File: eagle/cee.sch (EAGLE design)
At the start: 56 parts, among them IC1 IC1, J1 SOLDERJUMPERNC2

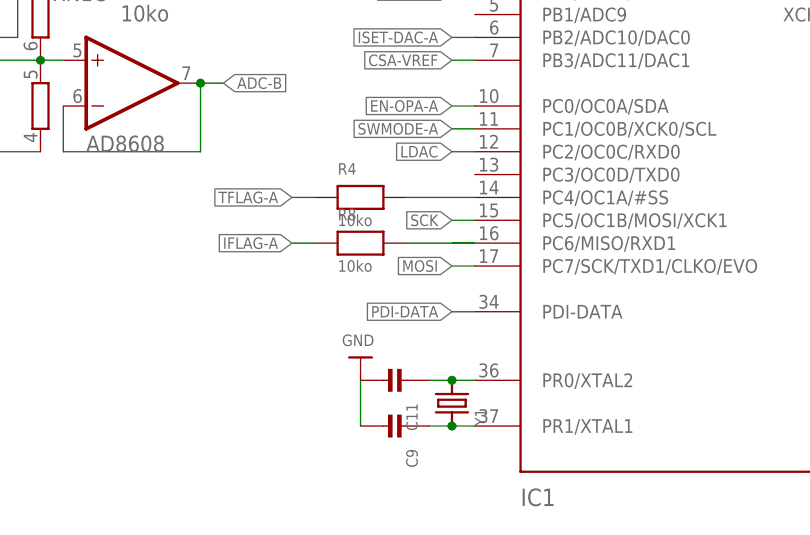
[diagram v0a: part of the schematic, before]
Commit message: Tweak expansion port labels.
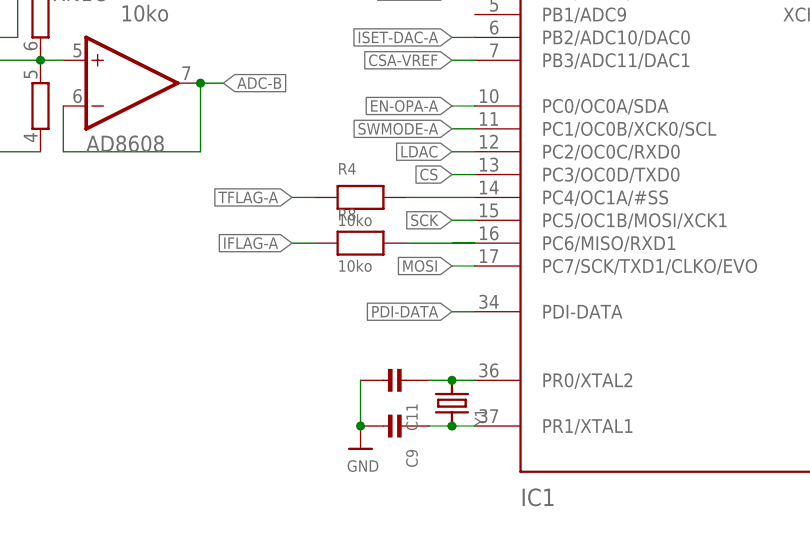
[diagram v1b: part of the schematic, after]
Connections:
- net CS: now also IC1.PC3/OC0D/TXD0
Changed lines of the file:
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@@
 <instance part="C9" gate="G$1" x="88.9" y="5.08" rot="R270"/>
 <instance part="C11" gate="G$1" x="88.9" y="10.16" rot="R270"/>
-<instance part="U$6" gate="G$1" x="86.36" y="12.7" rot="R180"/>
+<instance part="U$6" gate="G$1" x="86.36" y="2.54"/>
 <instance part="R1" gate="G$1" x="167.64" y="48.26" rot="R180"/>
 <instance part="R3" gate="G$1" x="167.64" y="50.8" rot="R180"/>
@@
 <label x="25.4" y="180.34" size="1.27" layer="95" rot="R180" xref="yes"/>
 </segment>
+<segment>
+<pinref part="IC1" gate="G$1" pin="PC3/OC0D/TXD0"/>
+<wire x1="99.06" y1="33.02" x2="96.52" y2="33.02" width="0.254" layer="91"/>
+<label x="96.52" y="33.02" size="1.27" layer="95" rot="R180" xref="yes"/>
+</segment>
 </net>
 <net name="SCK" class="0">
@@
 <pinref part="U$6" gate="G$1" pin="GND"/>
 <pinref part="C9" gate="G$1" pin="P$2"/>
+<junction x="86.36" y="5.08"/>
 <wire x1="86.36" y1="5.08" x2="86.36" y2="10.16" width="0.254" layer="91"/>
 </segment>

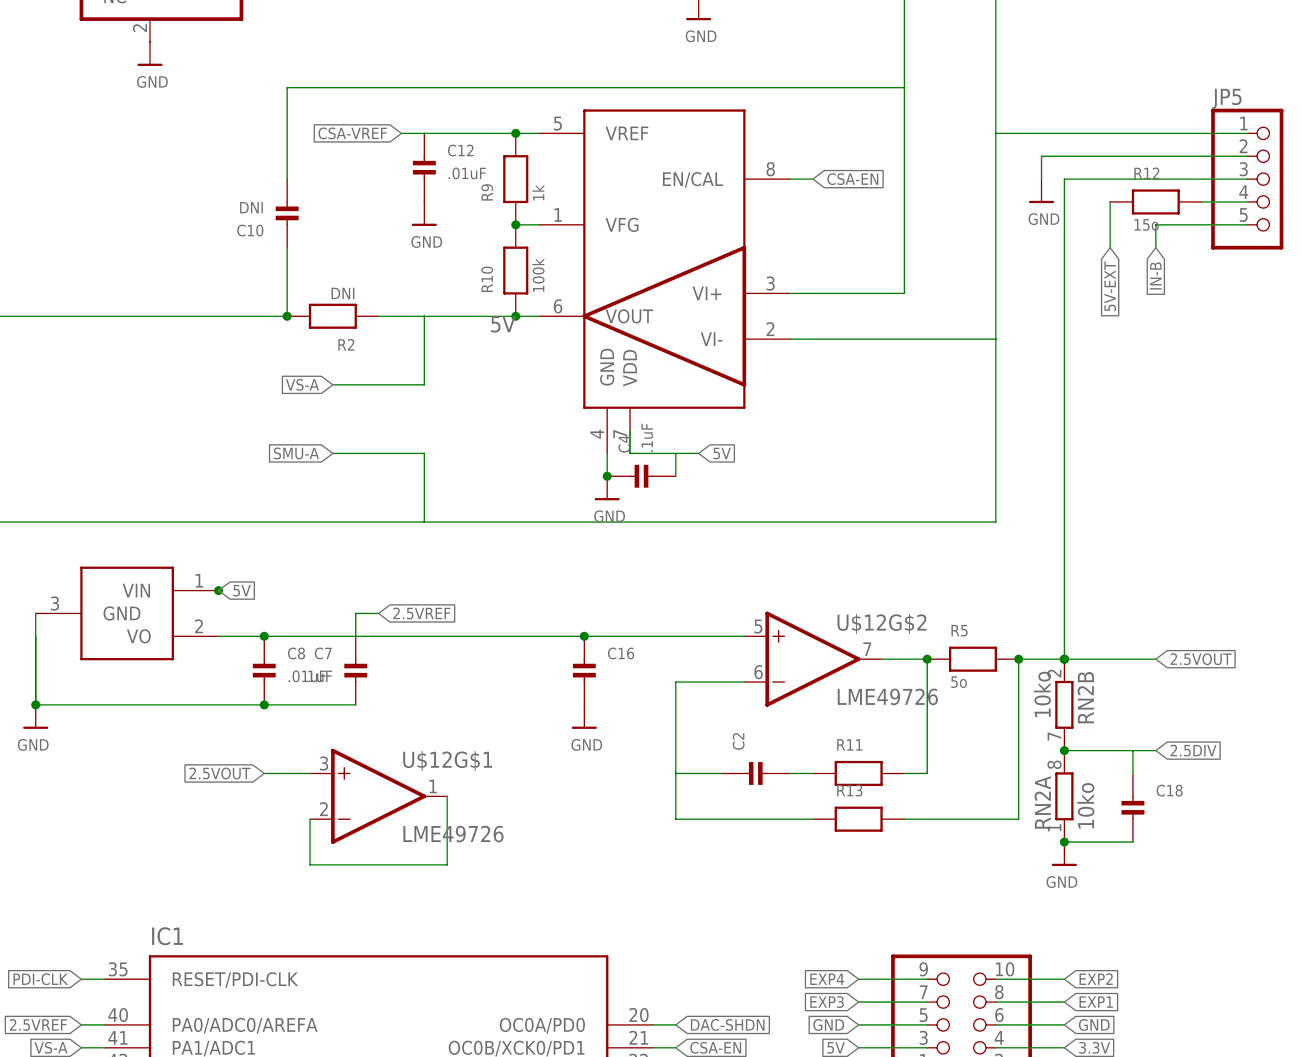
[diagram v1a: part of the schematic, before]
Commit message: Use LME49726 for current-limited 5V.
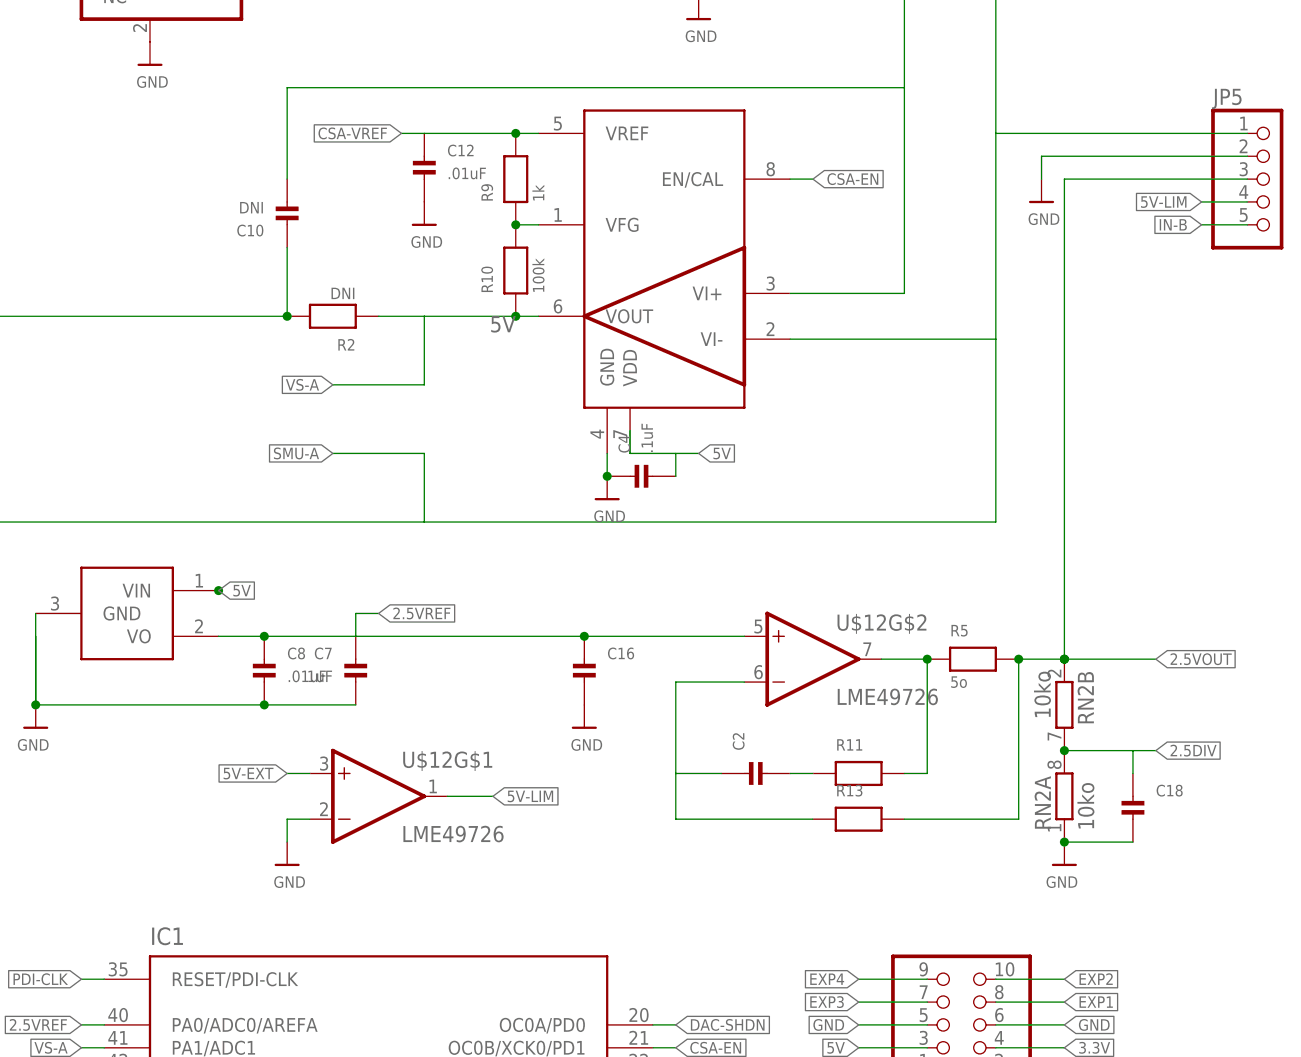
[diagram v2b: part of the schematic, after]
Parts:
- removed R12: 15o, nonolith:RESISTOR1206
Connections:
- removed net N$14: JP5.4, R12.2
- removed net N$15: U$12G$1.-IN, U$12G$1.OUT
- new net 5V-LIM: JP5.4, U$12G$1.OUT
- net 2.5VOUT: no longer U$12G$1.+IN
- net 5V-EXT: now also U$12G$1.+IN; no longer R12.1
- net GND: now also U$12G$1.-IN
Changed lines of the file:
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@@
 <part name="R11" library="nonolith" deviceset="RESISTOR" device="0603"/>
 <part name="C2" library="nonolith" deviceset="CAP_CERAMIC" device="0603"/>
-<part name="R12" library="nonolith" deviceset="RESISTOR" device="1206" value="15o"/>
 <part name="R13" library="nonolith" deviceset="RESISTOR" device="0603"/>
 <part name="R14" library="nonolith" deviceset="RESISTOR" device="0603" value="10k"/>
@@
 <part name="U$24" library="nonolith" deviceset="GND" device=""/>
 <part name="U$31" library="nonolith" deviceset="GND" device=""/>
+<part name="U$33" library="nonolith" deviceset="GND" device=""/>
 </parts>
 <sheets>
@@
 <instance part="R11" gate="G$1" x="182.88" y="106.68"/>
 <instance part="C2" gate="G$1" x="172.72" y="106.68" rot="R90"/>
-<instance part="R12" gate="G$1" x="215.9" y="170.18"/>
 <instance part="R13" gate="G$1" x="182.88" y="101.6"/>
 <instance part="R14" gate="G$1" x="86.36" y="198.12"/>
@@
 <instance part="RN2" gate="B" x="205.74" y="114.3" rot="R270"/>
 <instance part="U$31" gate="G$1" x="53.34" y="111.76"/>
+<instance part="U$33" gate="G$1" x="119.38" y="96.52"/>
 </instances>
 <busses>
@@
 <wire x1="27.94" y1="76.2" x2="25.4" y2="76.2" width="0.254" layer="91"/>
 </segment>
+<segment>
+<pinref part="U$12" gate="G$1" pin="-IN"/>
+<wire x1="121.92" y1="101.6" x2="119.38" y2="101.6" width="0.1524" layer="91"/>
+<wire x1="119.38" y1="101.6" x2="119.38" y2="99.06" width="0.1524" layer="91"/>
+<pinref part="U$33" gate="G$1" pin="GND"/>
+</segment>
 </net>
 <net name="PDI-DATA" class="0">
@@
 </segment>
 <segment>
-<pinref part="R12" gate="G$1" pin="1"/>
-<wire x1="210.82" y1="170.18" x2="210.82" y2="165.1" width="0.254" layer="91"/>
-<label x="210.82" y="165.1" size="1.27" layer="95" rot="R270" xref="yes"/>
+<pinref part="U$12" gate="G$1" pin="+IN"/>
+<wire x1="121.92" y1="106.68" x2="119.38" y2="106.68" width="0.1524" layer="91"/>
+<label x="119.38" y="106.68" size="1.27" layer="95" rot="R180" xref="yes"/>
 </segment>
 </net>
@@
 <junction x="205.74" y="119.38"/>
 </segment>
-<segment>
-<pinref part="U$12" gate="G$1" pin="+IN"/>
-<wire x1="121.92" y1="106.68" x2="116.84" y2="106.68" width="0.254" layer="91"/>
-<label x="116.84" y="106.68" size="1.27" layer="95" rot="R180" xref="yes"/>
-</segment>
 </net>
 <net name="2.5VFDBK" class="0">
@@
 <segment>
 <pinref part="JP5" gate="A" pin="5"/>
-<wire x1="226.06" y1="167.64" x2="215.9" y2="167.64" width="0.254" layer="91"/>
-<wire x1="215.9" y1="167.64" x2="215.9" y2="165.1" width="0.254" layer="91"/>
-<label x="215.9" y="165.1" size="1.27" layer="95" rot="R270" xref="yes"/>
+<wire x1="226.06" y1="167.64" x2="220.98" y2="167.64" width="0.254" layer="91"/>
+<label x="220.98" y="167.64" size="1.27" layer="95" rot="R180" xref="yes"/>
 </segment>
 <segment>
@@
 <pinref part="C2" gate="G$1" pin="P$2"/>
 <wire x1="177.8" y1="106.68" x2="175.26" y2="106.68" width="0.254" layer="91"/>
-</segment>
-</net>
-<net name="N$14" class="0">
-<segment>
-<pinref part="JP5" gate="A" pin="4"/>
-<wire x1="226.06" y1="170.18" x2="220.98" y2="170.18" width="0.254" layer="91"/>
-<pinref part="R12" gate="G$1" pin="2"/>
 </segment>
 </net>
@@
 </segment>
 </net>
-<net name="N$15" class="0">
-<segment>
-<pinref part="U$12" gate="G$1" pin="OUT"/>
-<wire x1="137.16" y1="104.14" x2="137.16" y2="96.52" width="0.254" layer="91"/>
-<pinref part="U$12" gate="G$1" pin="-IN"/>
-<wire x1="137.16" y1="96.52" x2="121.92" y2="96.52" width="0.254" layer="91"/>
-<wire x1="121.92" y1="96.52" x2="121.92" y2="101.6" width="0.254" layer="91"/>
-</segment>
-</net>
 <net name="BUFF-A" class="0">
 <segment>
@@
 </segment>
 </net>
+<net name="5V-LIM" class="0">
+<segment>
+<pinref part="U$12" gate="G$1" pin="OUT"/>
+<wire x1="137.16" y1="104.14" x2="142.24" y2="104.14" width="0.1524" layer="91"/>
+<label x="142.24" y="104.14" size="1.27" layer="95" xref="yes"/>
+</segment>
+<segment>
+<pinref part="JP5" gate="A" pin="4"/>
+<wire x1="226.06" y1="170.18" x2="220.98" y2="170.18" width="0.254" layer="91"/>
+<label x="220.98" y="170.18" size="1.27" layer="95" rot="R180" xref="yes"/>
+</segment>
+</net>

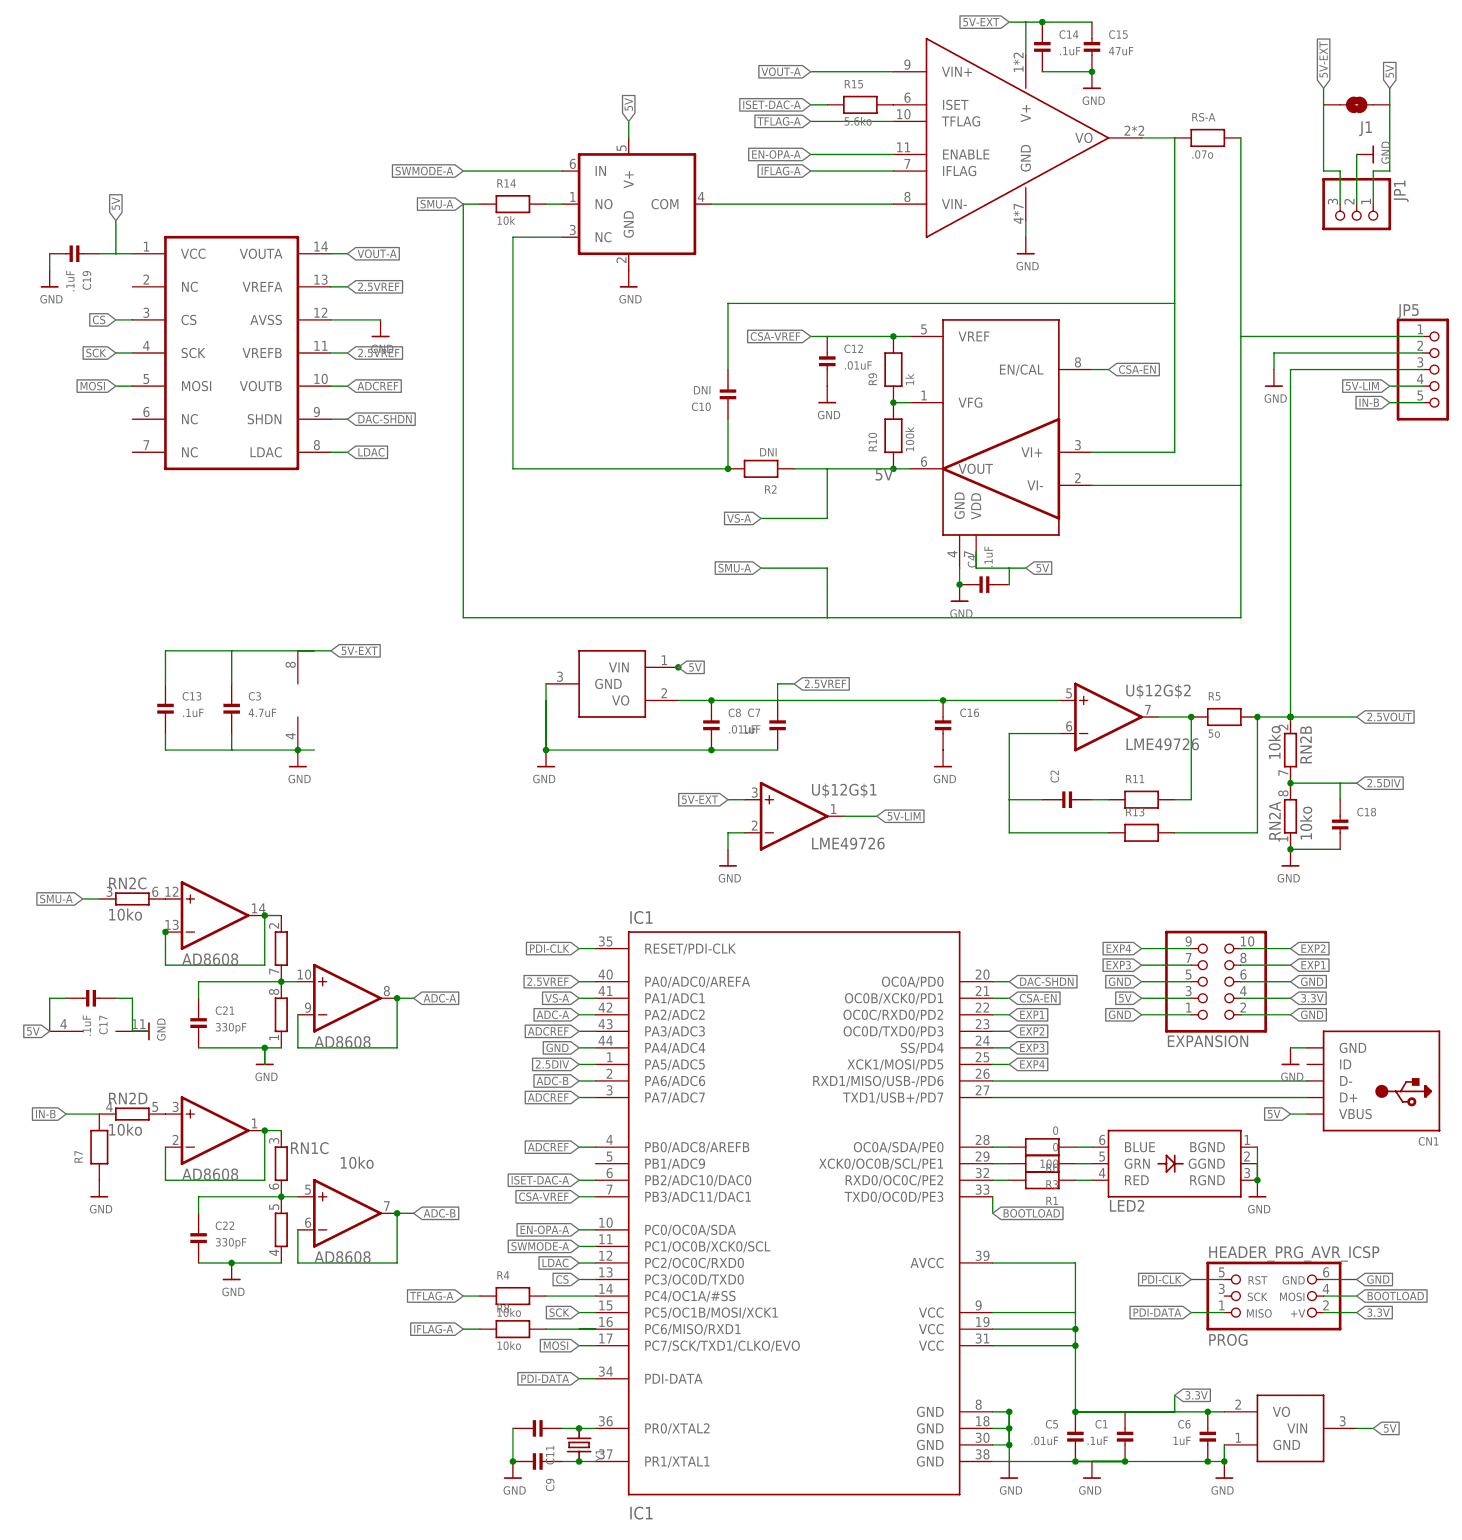
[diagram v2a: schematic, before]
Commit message: add junctions, leading zeroes, drop dangling 'o's
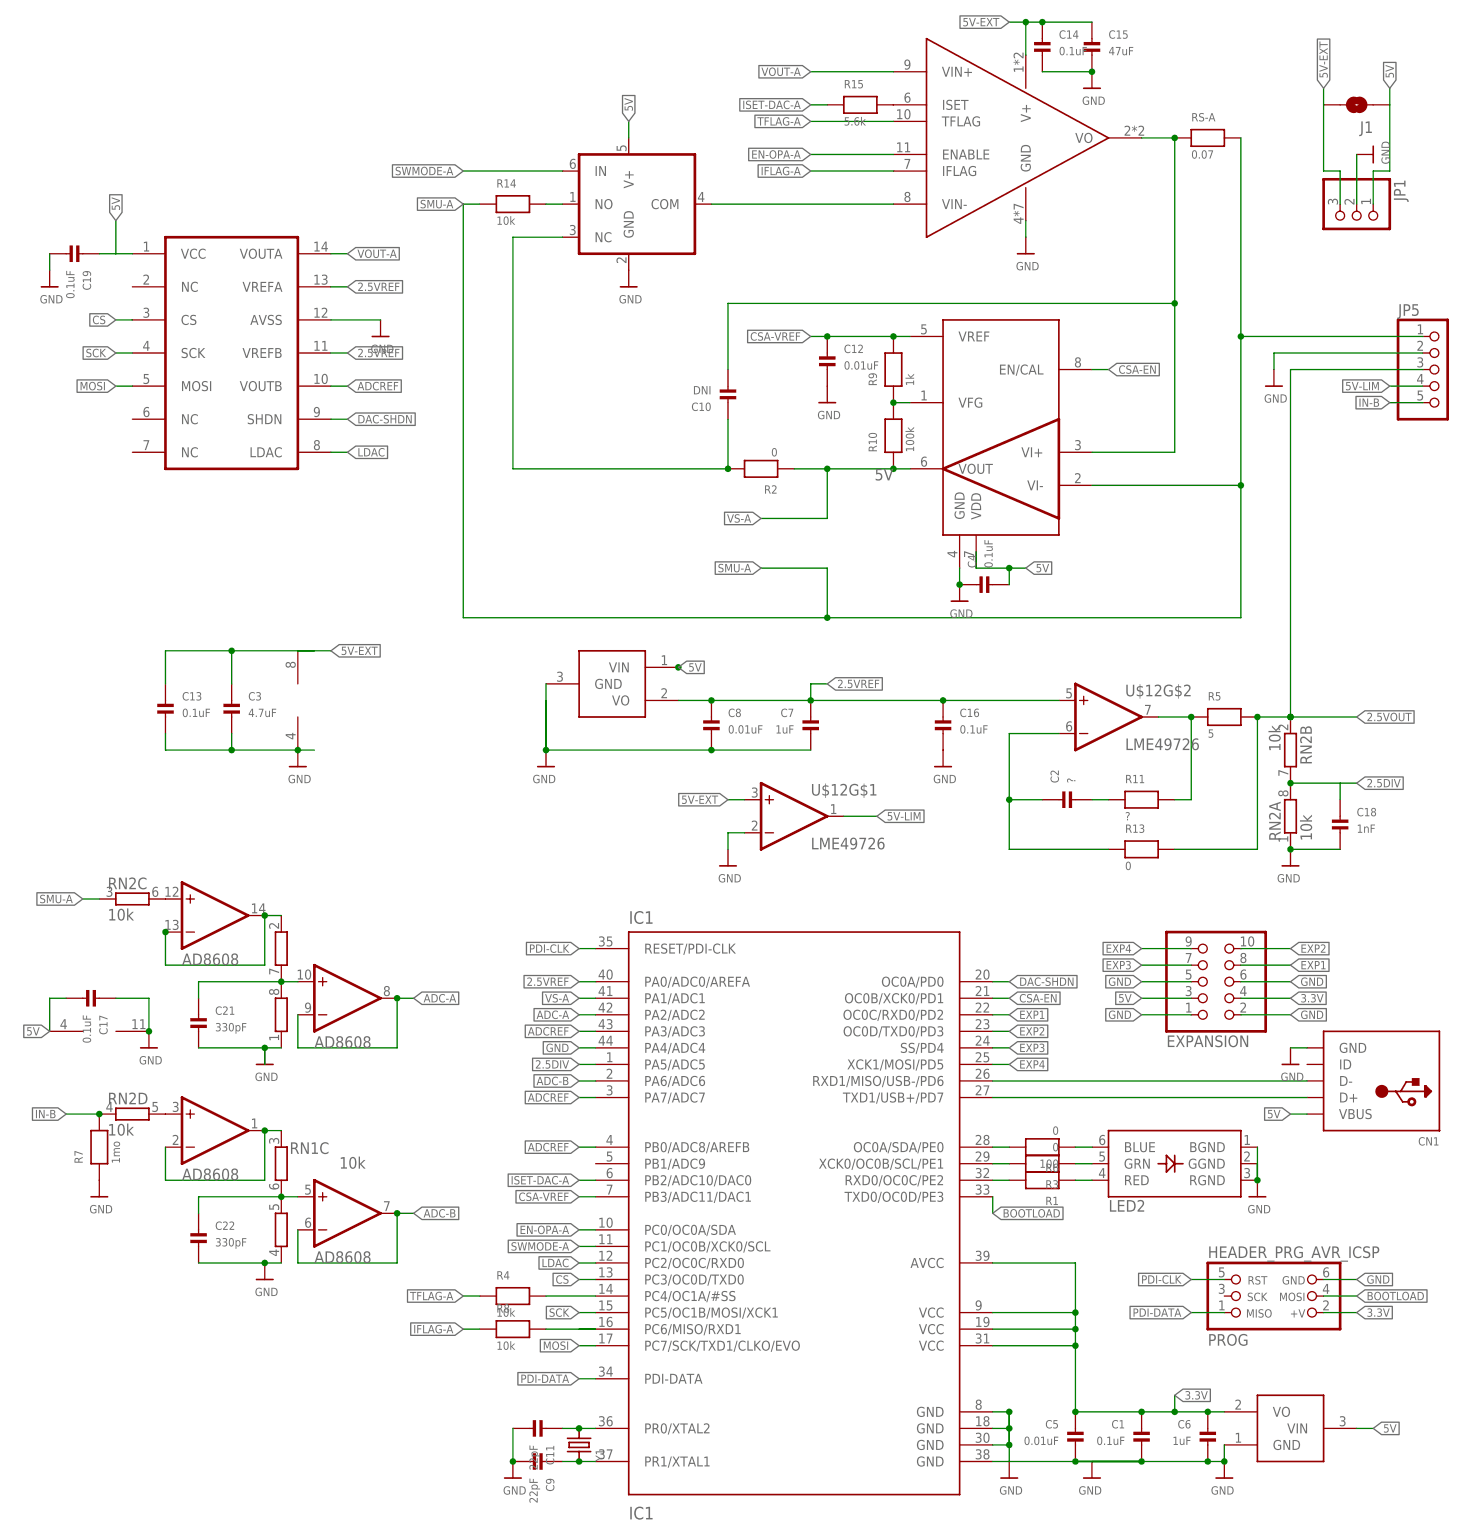
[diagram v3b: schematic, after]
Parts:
- C1, C13, C14, C17, C19, C4: value .1uF -> 0.1uF
- C11, C9: value (none) -> 22pF
- C12, C5, C8: value .01uF -> 0.01uF
- C16: value (none) -> 0.1uF
- C18: value (none) -> 1nF
- C2, R11: value (none) -> ?
- R13: value (none) -> 0
- R15: value 5.6ko -> 5.6k
- R2: value DNI -> 0
- R4, R8, RN1, RN2: value 10ko -> 10k
- R5: value 5o -> 5
- R7: value (none) -> 1mo
- RS-A: value .07o -> 0.07
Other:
- moved on the sheet: C1, C7, R13
